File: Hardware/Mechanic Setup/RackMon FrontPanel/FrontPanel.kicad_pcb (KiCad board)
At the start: 2 copper layers, 103 x 53 mm, 1 part

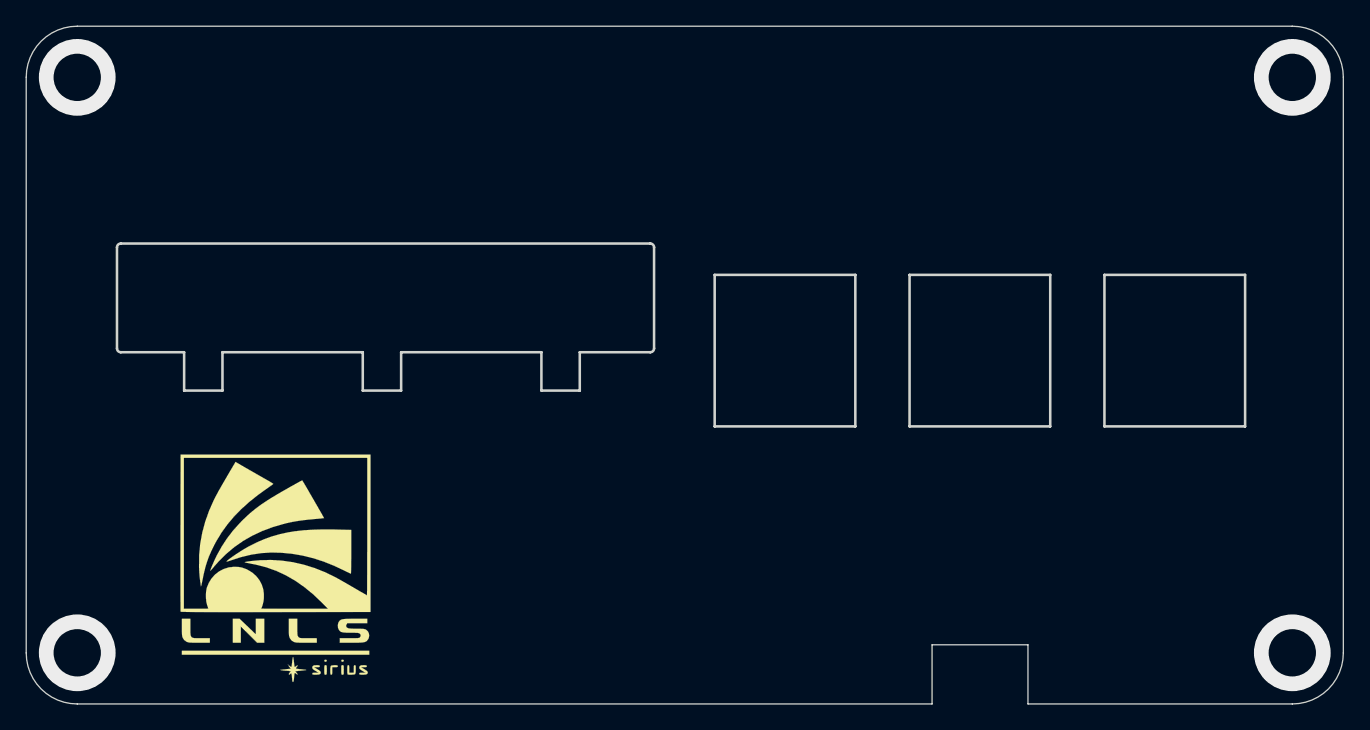
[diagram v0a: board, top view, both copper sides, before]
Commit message: 4P4C spacement adjusted
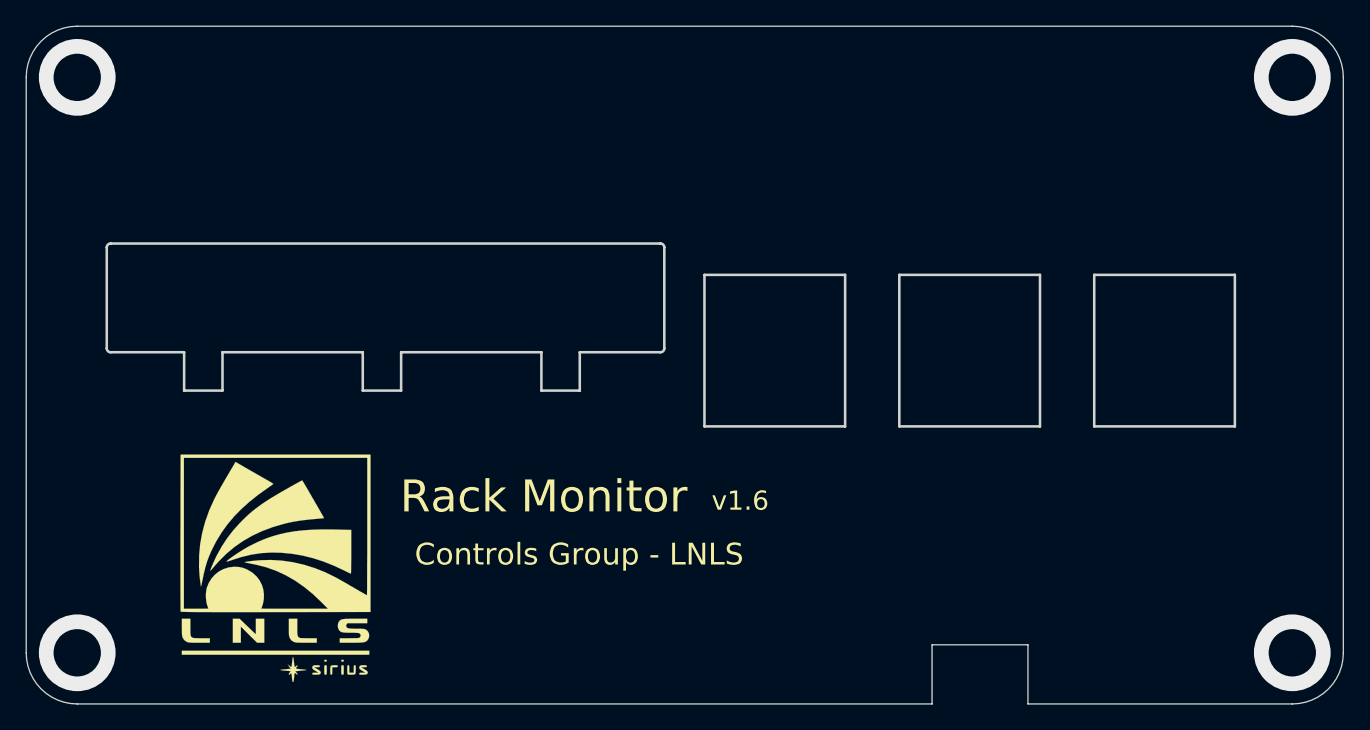
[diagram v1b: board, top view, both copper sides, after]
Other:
- outline, holes or cut-outs redrawn
- board text added: "Controls Group - LNLS"
- board text added: "Rack Monitor"
- board text added: "v1.6"
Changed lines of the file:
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@@
   (general
     (thickness 1.6)
-    (drawings 45)
+    (drawings 48)
     (tracks 4)
     (zones 0)
@@
       (xy 1.364287 7.214795)) (layer F.SilkS) (width 0.01))
   )
+  (gr_text "Controls Group - LNLS\n" (at 121.3206 120.5526) (layer F.SilkS)
+    (effects (font (size 1.7 1.7) (thickness 0.4)))
+  )
+  (gr_text "Rack Monitor\n" (at 118.552 116.0314) (layer F.SilkS)
+    (effects (font (size 2.5 2.5) (thickness 0.5)))
+  )
+  (gr_text v1.6 (at 133.919 116.3616) (layer F.SilkS)
+    (effects (font (size 1.5 1.5) (thickness 0.2)))
+  )
   (gr_line (start 156.42 132.24527) (end 177.09123 132.24527) (layer Edge.Cuts) (width 0.1))
   (gr_line (start 156.42 127.62) (end 156.42 132.24527) (layer Edge.Cuts) (width 0.1))
@@
   (gr_line (start 148.92 127.62) (end 156.42 127.62) (layer Edge.Cuts) (width 0.1))
   (gr_line (start 152.67 132.12) (end 152.67 131.9) (layer Cmts.User) (width 0.15))
-  (gr_line (start 85.18 104.44) (end 85.18 96.54) (layer Edge.Cuts) (width 0.2))
-  (gr_line (start 127.18 96.54) (end 127.18 104.44) (layer Edge.Cuts) (width 0.2))
-  (gr_arc (start 126.88 96.54) (end 127.18 96.54) (angle -90) (layer Edge.Cuts) (width 0.2))
-  (gr_line (start 85.48 104.74) (end 90.43 104.74) (layer Edge.Cuts) (width 0.2))
-  (gr_line (start 126.88 104.74) (end 121.37 104.74) (layer Edge.Cuts) (width 0.2))
-  (gr_line (start 126.88 96.24) (end 85.48 96.24) (layer Edge.Cuts) (width 0.2))
-  (gr_arc (start 126.88 104.44) (end 127.18 104.44) (angle 90) (layer Edge.Cuts) (width 0.2))
-  (gr_arc (start 85.48 104.44) (end 85.48 104.74) (angle 90) (layer Edge.Cuts) (width 0.2))
-  (gr_arc (start 85.48 96.54) (end 85.18 96.54) (angle 90) (layer Edge.Cuts) (width 0.2))
+  (gr_line (start 84.38 104.44) (end 84.38 96.54) (layer Edge.Cuts) (width 0.2))
+  (gr_line (start 127.98 96.54) (end 127.98 104.44) (layer Edge.Cuts) (width 0.2))
+  (gr_arc (start 127.68 96.54) (end 127.98 96.54) (angle -90) (layer Edge.Cuts) (width 0.2))
+  (gr_line (start 84.68 104.74) (end 90.43 104.74) (layer Edge.Cuts) (width 0.2))
+  (gr_line (start 127.68 104.74) (end 121.37 104.74) (layer Edge.Cuts) (width 0.2))
+  (gr_line (start 127.68 96.24) (end 84.68 96.24) (layer Edge.Cuts) (width 0.2))
+  (gr_arc (start 127.68 104.44) (end 127.98 104.44) (angle 90) (layer Edge.Cuts) (width 0.2))
+  (gr_arc (start 84.68 104.44) (end 84.68 104.74) (angle 90) (layer Edge.Cuts) (width 0.2))
+  (gr_arc (start 84.68 96.54) (end 84.38 96.54) (angle 90) (layer Edge.Cuts) (width 0.2))
   (gr_line (start 104.4 104.74) (end 93.43 104.74) (layer Edge.Cuts) (width 0.2))
   (gr_line (start 118.37 104.74) (end 107.4 104.74) (layer Edge.Cuts) (width 0.2))
@@
   (gr_line (start 90.43 107.74) (end 93.43 107.74) (layer Edge.Cuts) (width 0.2))
   (gr_line (start 90.43 104.74) (end 90.43 107.74) (layer Edge.Cuts) (width 0.2))
-  (gr_line (start 131.92 110.54) (end 142.92 110.54) (layer Edge.Cuts) (width 0.2))
-  (gr_line (start 142.92 110.54) (end 142.92 98.69) (layer Edge.Cuts) (width 0.2))
-  (gr_line (start 131.92 98.69) (end 131.92 110.54) (layer Edge.Cuts) (width 0.2))
-  (gr_line (start 147.16 110.54) (end 158.16 110.54) (layer Edge.Cuts) (width 0.2))
-  (gr_line (start 158.16 110.54) (end 158.16 98.69) (layer Edge.Cuts) (width 0.2))
-  (gr_line (start 147.16 98.69) (end 147.16 110.54) (layer Edge.Cuts) (width 0.2))
-  (gr_line (start 142.92 98.69) (end 131.92 98.69) (layer Edge.Cuts) (width 0.2))
-  (gr_line (start 158.16 98.69) (end 147.16 98.69) (layer Edge.Cuts) (width 0.2))
-  (gr_line (start 173.4 110.54) (end 173.4 98.69) (layer Edge.Cuts) (width 0.2))
-  (gr_line (start 162.4 110.54) (end 173.4 110.54) (layer Edge.Cuts) (width 0.2))
-  (gr_line (start 162.4 98.69) (end 162.4 110.54) (layer Edge.Cuts) (width 0.2))
-  (gr_line (start 173.4 98.69) (end 162.4 98.69) (layer Edge.Cuts) (width 0.2))
+  (gr_line (start 131.12 110.54) (end 142.12 110.54) (layer Edge.Cuts) (width 0.2))
+  (gr_line (start 142.12 110.54) (end 142.12 98.69) (layer Edge.Cuts) (width 0.2))
+  (gr_line (start 131.12 98.69) (end 131.12 110.54) (layer Edge.Cuts) (width 0.2))
+  (gr_line (start 146.36 110.54) (end 157.36 110.54) (layer Edge.Cuts) (width 0.2))
+  (gr_line (start 157.36 110.54) (end 157.36 98.69) (layer Edge.Cuts) (width 0.2))
+  (gr_line (start 146.36 98.69) (end 146.36 110.54) (layer Edge.Cuts) (width 0.2))
+  (gr_line (start 142.12 98.69) (end 131.12 98.69) (layer Edge.Cuts) (width 0.2))
+  (gr_line (start 157.36 98.69) (end 146.36 98.69) (layer Edge.Cuts) (width 0.2))
+  (gr_line (start 172.6 110.54) (end 172.6 98.69) (layer Edge.Cuts) (width 0.2))
+  (gr_line (start 161.6 110.54) (end 172.6 110.54) (layer Edge.Cuts) (width 0.2))
+  (gr_line (start 161.6 98.69) (end 161.6 110.54) (layer Edge.Cuts) (width 0.2))
+  (gr_line (start 172.6 98.69) (end 161.6 98.69) (layer Edge.Cuts) (width 0.2))
   (gr_line (start 148.92 132.24527) (end 82.07123 132.24527) (layer Edge.Cuts) (width 0.1))
   (gr_arc (start 82.07123 128.25527) (end 82.07123 132.24527) (angle 90) (layer Edge.Cuts) (width 0.1))
